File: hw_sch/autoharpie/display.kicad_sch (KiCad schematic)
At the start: 41 parts, among them J5 Conn_01x04_Socket, SW1 RotaryEncoder_Switch, SW19 SW_Push, SW2 RotaryEncoder, SW20 SW_Push, SW21 SW_Push, SW75 RotaryEncoder, SW76 RotaryEncoder

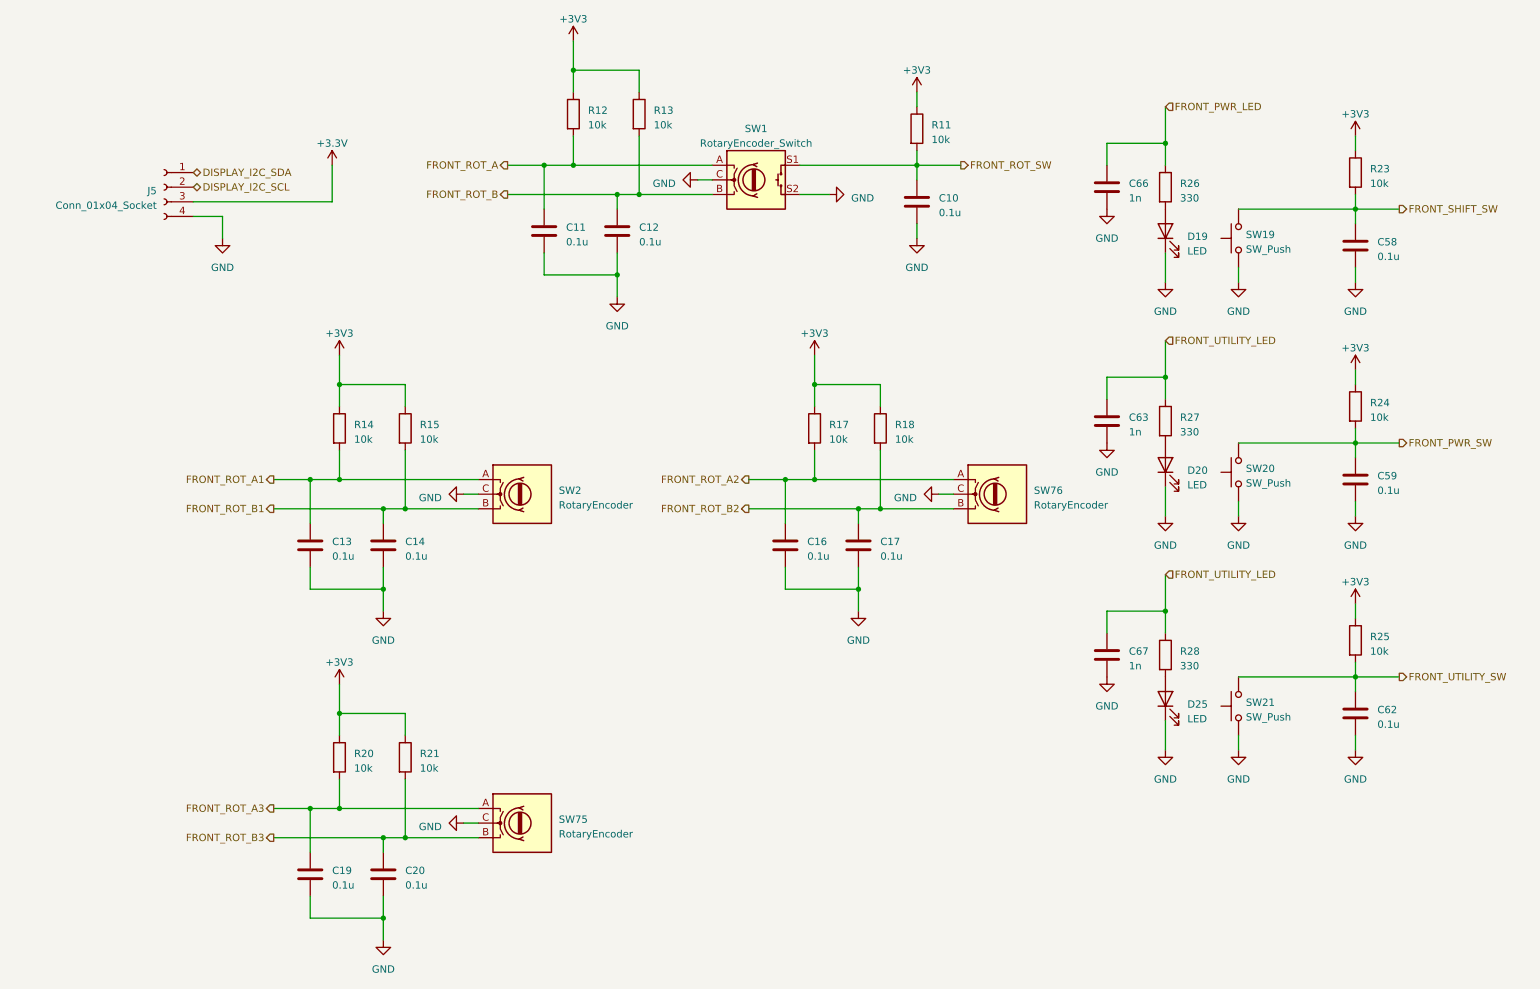
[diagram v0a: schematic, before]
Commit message: DAC wiring, add heirch pins
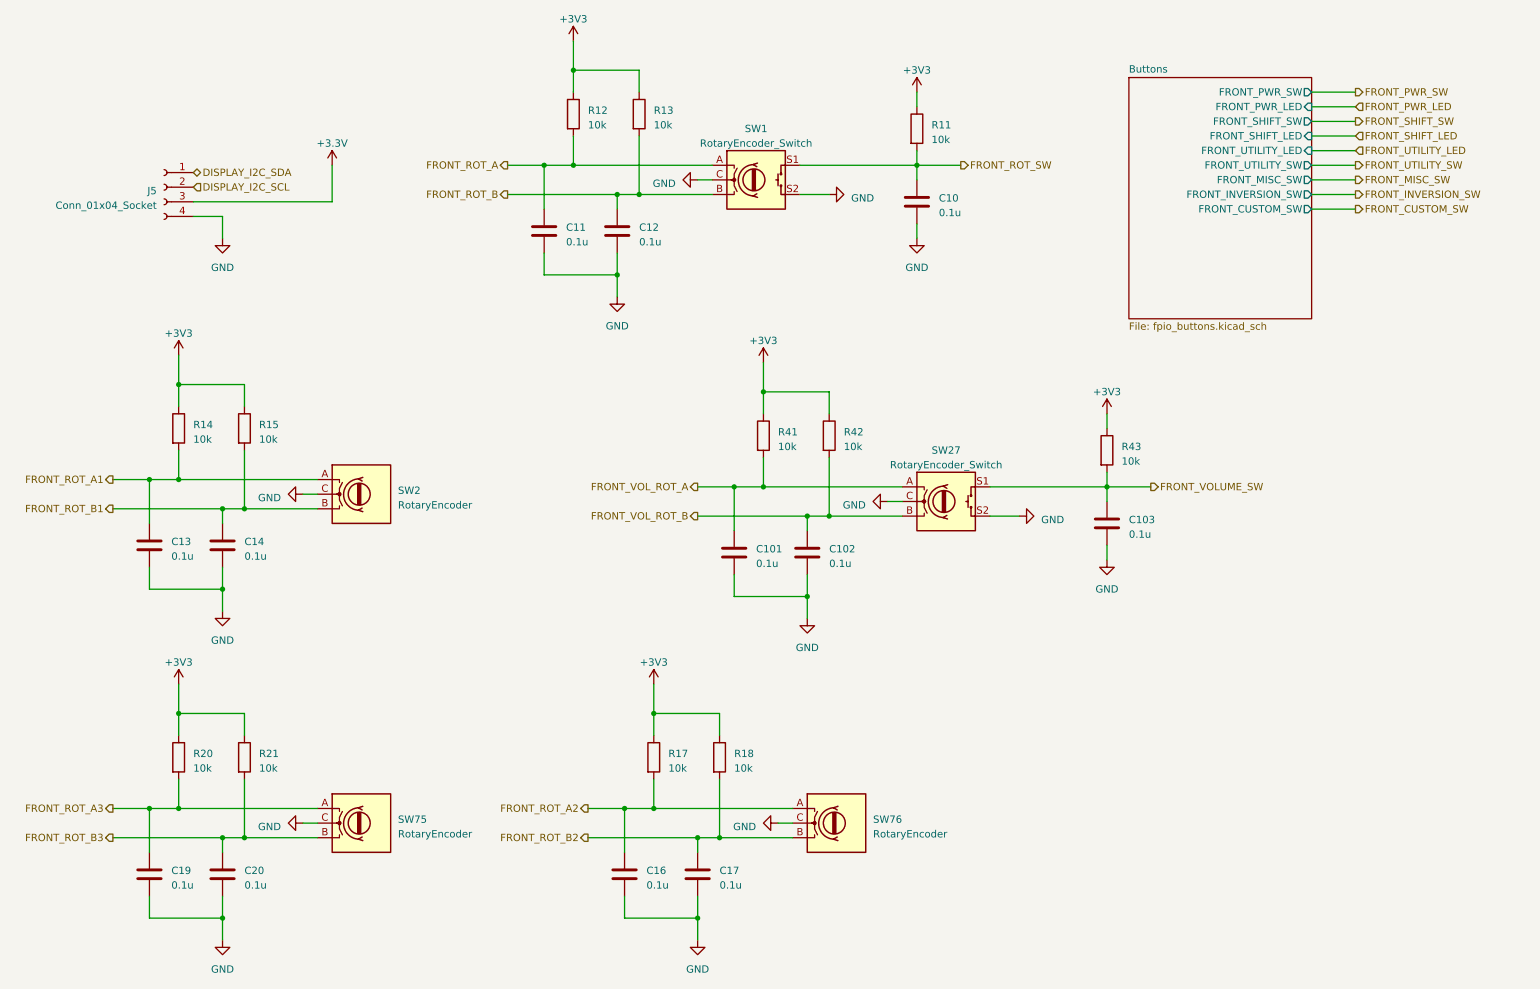
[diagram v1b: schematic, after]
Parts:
- removed C58, C59, C62: 0.1u, symbol Device:C
- removed C63, C66, C67: 1n, symbol Device:C
- removed D19, D20, D25: LED, symbol Device:LED
- removed R23, R24, R25: 10k, symbol Device:R
- removed R26, R27, R28: 330, symbol Device:R
- removed SW19, SW20, SW21: SW_Push, symbol Switch:SW_Push
- added C101, C102, C103: 0.1u, symbol Device:C
- added R41, R42, R43: 10k, symbol Device:R
- added SW27: RotaryEncoder_Switch, symbol Device:RotaryEncoder_Switch
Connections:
- net +3V3: now also R41.1, R42.1, R43.1
- net GND: now also C101.2, C102.2, C103.2, SW27.C, SW27.S2
- new net FRONT_VOLUME_SW: C103.1, R43.2, SW27.S1
- new net FRONT_VOL_ROT_A: C101.1, R41.2, SW27.A
- new net FRONT_VOL_ROT_B: C102.1, R42.2, SW27.B
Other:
- added sheet Buttons (fpio_buttons.kicad_sch)
- moved on the sheet: C13, C14, C16, C17, C19, C20, R14, R15, R17, R18, R20, R21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

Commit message: keypad
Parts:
- removed C101, C102, C103, C13, C14, C16, C17, C19, C20: 0.1u, symbol Device:C
- removed R14, R15, R17, R18, R20, R21, R41, R42, R43: 10k, symbol Device:R
- removed SW2, SW75, SW76: RotaryEncoder, symbol Device:RotaryEncoder
- removed SW27: RotaryEncoder_Switch, symbol Device:RotaryEncoder_Switch
- added C26, C28, C33: 1n, Capacitor_SMD:C_0402_1005Metric, symbol Device:C
- added C27, C29: 0.1u, Capacitor_SMD:C_0402_1005Metric, symbol Device:C
- added D4, D5, D6: LED, LED_THT:LED_D3.0mm, symbol Device:LED
- added R26, R28: 10k, Resistor_THT:R_Axial_DIN0204_L3.6mm_D1.6mm_P7.62mm_Horizontal, symbol Device:R
- added R27, R29, R33: 330, Resistor_THT:R_Axial_DIN0204_L3.6mm_D1.6mm_P7.62mm_Horizontal, symbol Device:R
- added SW1, SW2: SW_Push, Button_Switch_THT:SW_PUSH_6mm_H4.3mm, symbol Switch:SW_Push
- C30: renamed from C10; footprint (none) -> Capacitor_SMD:C_0402_1005Metric
- C31: renamed from C11; footprint (none) -> Capacitor_SMD:C_0402_1005Metric
- C32: renamed from C12; footprint (none) -> Capacitor_SMD:C_0402_1005Metric
- J6: renamed from J5; footprint Display:OLED-128O064D -> Connector_PinSocket_2.54mm:PinSocket_1x04_P2.54mm_Vertical
- R30: renamed from R12; footprint (none) -> Resistor_THT:R_Axial_DIN0204_L3.6mm_D1.6mm_P7.62mm_Horizontal
- R31: renamed from R13; footprint (none) -> Resistor_THT:R_Axial_DIN0204_L3.6mm_D1.6mm_P7.62mm_Horizontal
- R32: renamed from R11; footprint (none) -> Resistor_THT:R_Axial_DIN0204_L3.6mm_D1.6mm_P7.62mm_Horizontal
- SW3: renamed from SW1; footprint (none) -> Rotary_Encoder:RotaryEncoder_Alps_EC11E-Switch_Vertical_H20mm
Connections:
- net +3V3: now also R26.1, R28.1
- net FRONT_PWR_LED: now also C28.1, R29.1
- net FRONT_PWR_SW: now also C29.1, R28.2, SW2.2
- net FRONT_SHIFT_LED: now also C26.1, R27.1
- net FRONT_SHIFT_SW: now also C27.1, R26.2, SW1.2
- net FRONT_UTILITY_LED: now also C33.1, R33.1
- net GND: now also C26.2, C27.2, C28.2, C29.2, C33.2, D4.1 (K), D5.1 (K), D6.1 (K), SW1.1, SW2.1
- new net: D5.2 (A), R29.2
- new net: D6.2 (A), R33.2
- new net: D4.2 (A), R27.2
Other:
- removed sheet Buttons
- moved on the sheet: C30, C31, C32, R30, R31, R32, SW3

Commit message: rev 0.1 pcb
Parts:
- removed C26, C28, C33: 1n, Capacitor_SMD:C_0402_1005Metric, symbol Device:C
- removed C27, C29, C30, C31, C32: 0.1u, Capacitor_SMD:C_0402_1005Metric, symbol Device:C
- removed D4, D5, D6: LED, LED_THT:LED_D3.0mm, symbol Device:LED
- removed R26, R28: 10k, Resistor_THT:R_Axial_DIN0204_L3.6mm_D1.6mm_P7.62mm_Horizontal, symbol Device:R
- removed R27, R29, R33: 330, Resistor_THT:R_Axial_DIN0204_L3.6mm_D1.6mm_P7.62mm_Horizontal, symbol Device:R
- removed SW1, SW2: SW_Push, Button_Switch_THT:SW_PUSH_6mm_H4.3mm, symbol Switch:SW_Push
- renumbered J6 to J4, R30 to R10, R31 to R11, R32 to R12, SW3 to SW1
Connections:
- net +3.3V is gone; now on net DISPLAY_I2C_SCL: J4.3 (Pin_3)
- net +3V3: now also J4.2 (Pin_2)
- net DISPLAY_I2C_SCL: no longer J4.2 (Pin_2)
- net DISPLAY_I2C_SDA: now also J4.4 (Pin_4); no longer J4.1 (Pin_1)
- net GND: now also J4.1 (Pin_1); no longer J4.4 (Pin_4)

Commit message: ic fix atept
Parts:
- SW2: renamed from SW1; footprint Rotary_Encoder:RotaryEncoder_Alps_EC11E-Switch_Vertical_H20mm -> Rotary_Encoder:RotaryEncoder_Bourns_Vertical_PEC12R-3xxxF-Sxxxx
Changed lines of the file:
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@@
   (symbol (lib_id "power:GND") (at 77.47 100.33 270) (unit 1)
     (in_bom yes) (on_board yes) (dnp no) (fields_autoplaced)
-    (property "Reference" "#PWR045" (at 71.12 100.33 0)
+    (property "Reference" "#PWR047" (at 71.12 100.33 0)
       (effects (font (size 1.27 1.27)) hide)
     )
@@
       (project "autoharpie"
         (path "/f22a88c4-866b-40a0-9fc2-96344be0ec71/b98961c6-5a9e-45f8-94a5-02c3a7ae5bfc"
+          (reference "#PWR047") (unit 1)
+        )
+      )
+    )
+  )
+  (symbol (lib_id "power:+3V3") (at 45.72 48.26 270) (unit 1)
+    (in_bom yes) (on_board yes) (dnp no) (fields_autoplaced)
+    (property "Reference" "#PWR044" (at 41.91 48.26 0)
+      (effects (font (size 1.27 1.27)) hide)
+    )
+    (property "Value" "+3V3" (at 49.53 48.895 90)
+      (effects (font (size 1.27 1.27)) (justify left))
+    )
+    (property "Footprint" "" (at 45.72 48.26 0)
+      (effects (font (size 1.27 1.27)) hide)
+    )
+    (property "Datasheet" "" (at 45.72 48.26 0)
+      (effects (font (size 1.27 1.27)) hide)
+    )
+    (pin "1")
+    (instances
+      (project "autoharpie"
+        (path "/f22a88c4-866b-40a0-9fc2-96344be0ec71/b98961c6-5a9e-45f8-94a5-02c3a7ae5bfc"
+          (reference "#PWR044") (unit 1)
+        )
+      )
+    )
+  )
+  (symbol (lib_id "Device:R") (at 55.88 88.9 0) (unit 1)
+    (in_bom yes) (on_board yes) (dnp no) (fields_autoplaced)
+    (property "Reference" "R10" (at 58.42 88.265 0)
+      (effects (font (size 1.27 1.27)) (justify left))
+    )
+    (property "Value" "10k" (at 58.42 90.805 0)
+      (effects (font (size 1.27 1.27)) (justify left))
+    )
+    (property "Footprint" "Resistor_THT:R_Axial_DIN0204_L3.6mm_D1.6mm_P7.62mm_Horizontal" (at 54.102 88.9 90)
+      (effects (font (size 1.27 1.27)) hide)
+    )
+    (property "Datasheet" "~" (at 55.88 88.9 0)
+      (effects (font (size 1.27 1.27)) hide)
+    )
+    (pin "1")
+    (pin "2")
+    (instances
+      (project "autoharpie"
+        (path "/f22a88c4-866b-40a0-9fc2-96344be0ec71/b98961c6-5a9e-45f8-94a5-02c3a7ae5bfc"
+          (reference "R10") (unit 1)
+        )
+      )
+    )
+  )
+  (symbol (lib_id "Device:R") (at 67.31 88.9 0) (unit 1)
+    (in_bom yes) (on_board yes) (dnp no) (fields_autoplaced)
+    (property "Reference" "R11" (at 69.85 88.265 0)
+      (effects (font (size 1.27 1.27)) (justify left))
+    )
+    (property "Value" "10k" (at 69.85 90.805 0)
+      (effects (font (size 1.27 1.27)) (justify left))
+    )
+    (property "Footprint" "Resistor_THT:R_Axial_DIN0204_L3.6mm_D1.6mm_P7.62mm_Horizontal" (at 65.532 88.9 90)
+      (effects (font (size 1.27 1.27)) hide)
+    )
+    (property "Datasheet" "~" (at 67.31 88.9 0)
+      (effects (font (size 1.27 1.27)) hide)
+    )
+    (pin "1")
+    (pin "2")
+    (instances
+      (project "autoharpie"
+        (path "/f22a88c4-866b-40a0-9fc2-96344be0ec71/b98961c6-5a9e-45f8-94a5-02c3a7ae5bfc"
+          (reference "R11") (unit 1)
+        )
+      )
+    )
+  )
+  (symbol (lib_id "power:+3V3") (at 55.88 76.2 0) (unit 1)
+    (in_bom yes) (on_board yes) (dnp no) (fields_autoplaced)
+    (property "Reference" "#PWR045" (at 55.88 80.01 0)
+      (effects (font (size 1.27 1.27)) hide)
+    )
+    (property "Value" "+3V3" (at 55.88 72.39 0)
+      (effects (font (size 1.27 1.27)))
+    )
+    (property "Footprint" "" (at 55.88 76.2 0)
+      (effects (font (size 1.27 1.27)) hide)
+    )
+    (property "Datasheet" "" (at 55.88 76.2 0)
+      (effects (font (size 1.27 1.27)) hide)
+    )
+    (pin "1")
+    (instances
+      (project "autoharpie"
+        (path "/f22a88c4-866b-40a0-9fc2-96344be0ec71/b98961c6-5a9e-45f8-94a5-02c3a7ae5bfc"
           (reference "#PWR045") (unit 1)
         )
@@
     )
   )
-  (symbol (lib_id "power:+3V3") (at 45.72 48.26 270) (unit 1)
-    (in_bom yes) (on_board yes) (dnp no) (fields_autoplaced)
-    (property "Reference" "#PWR042" (at 41.91 48.26 0)
-      (effects (font (size 1.27 1.27)) hide)
-    )
-    (property "Value" "+3V3" (at 49.53 48.895 90)
-      (effects (font (size 1.27 1.27)) (justify left))
-    )
-    (property "Footprint" "" (at 45.72 48.26 0)
-      (effects (font (size 1.27 1.27)) hide)
-    )
-    (property "Datasheet" "" (at 45.72 48.26 0)
-      (effects (font (size 1.27 1.27)) hide)
-    )
-    (pin "1")
-    (instances
-      (project "autoharpie"
-        (path "/f22a88c4-866b-40a0-9fc2-96344be0ec71/b98961c6-5a9e-45f8-94a5-02c3a7ae5bfc"
-          (reference "#PWR042") (unit 1)
-        )
-      )
-    )
-  )
-  (symbol (lib_id "Device:R") (at 55.88 88.9 0) (unit 1)
-    (in_bom yes) (on_board yes) (dnp no) (fields_autoplaced)
-    (property "Reference" "R10" (at 58.42 88.265 0)
-      (effects (font (size 1.27 1.27)) (justify left))
-    )
-    (property "Value" "10k" (at 58.42 90.805 0)
-      (effects (font (size 1.27 1.27)) (justify left))
-    )
-    (property "Footprint" "Resistor_THT:R_Axial_DIN0204_L3.6mm_D1.6mm_P7.62mm_Horizontal" (at 54.102 88.9 90)
-      (effects (font (size 1.27 1.27)) hide)
-    )
-    (property "Datasheet" "~" (at 55.88 88.9 0)
-      (effects (font (size 1.27 1.27)) hide)
-    )
-    (pin "1")
-    (pin "2")
-    (instances
-      (project "autoharpie"
-        (path "/f22a88c4-866b-40a0-9fc2-96344be0ec71/b98961c6-5a9e-45f8-94a5-02c3a7ae5bfc"
-          (reference "R10") (unit 1)
-        )
-      )
-    )
-  )
-  (symbol (lib_id "Device:R") (at 67.31 88.9 0) (unit 1)
-    (in_bom yes) (on_board yes) (dnp no) (fields_autoplaced)
-    (property "Reference" "R11" (at 69.85 88.265 0)
-      (effects (font (size 1.27 1.27)) (justify left))
-    )
-    (property "Value" "10k" (at 69.85 90.805 0)
-      (effects (font (size 1.27 1.27)) (justify left))
-    )
-    (property "Footprint" "Resistor_THT:R_Axial_DIN0204_L3.6mm_D1.6mm_P7.62mm_Horizontal" (at 65.532 88.9 90)
-      (effects (font (size 1.27 1.27)) hide)
-    )
-    (property "Datasheet" "~" (at 67.31 88.9 0)
-      (effects (font (size 1.27 1.27)) hide)
-    )
-    (pin "1")
-    (pin "2")
-    (instances
-      (project "autoharpie"
-        (path "/f22a88c4-866b-40a0-9fc2-96344be0ec71/b98961c6-5a9e-45f8-94a5-02c3a7ae5bfc"
-          (reference "R11") (unit 1)
-        )
-      )
-    )
-  )
-  (symbol (lib_id "power:+3V3") (at 55.88 76.2 0) (unit 1)
-    (in_bom yes) (on_board yes) (dnp no) (fields_autoplaced)
-    (property "Reference" "#PWR043" (at 55.88 80.01 0)
-      (effects (font (size 1.27 1.27)) hide)
-    )
-    (property "Value" "+3V3" (at 55.88 72.39 0)
-      (effects (font (size 1.27 1.27)))
-    )
-    (property "Footprint" "" (at 55.88 76.2 0)
-      (effects (font (size 1.27 1.27)) hide)
-    )
-    (property "Datasheet" "" (at 55.88 76.2 0)
-      (effects (font (size 1.27 1.27)) hide)
-    )
-    (pin "1")
-    (instances
-      (project "autoharpie"
-        (path "/f22a88c4-866b-40a0-9fc2-96344be0ec71/b98961c6-5a9e-45f8-94a5-02c3a7ae5bfc"
-          (reference "#PWR043") (unit 1)
-        )
-      )
-    )
-  )
   (symbol (lib_id "Device:RotaryEncoder_Switch") (at 87.63 100.33 0) (unit 1)
     (in_bom yes) (on_board yes) (dnp no) (fields_autoplaced)
-    (property "Reference" "SW1" (at 87.63 91.44 0)
+    (property "Reference" "SW2" (at 87.63 91.44 0)
       (effects (font (size 1.27 1.27)))
     )
@@
       (effects (font (size 1.27 1.27)))
     )
-    (property "Footprint" "Rotary_Encoder:RotaryEncoder_Alps_EC11E-Switch_Vertical_H20mm" (at 83.82 96.266 0)
+    (property "Footprint" "Rotary_Encoder:RotaryEncoder_Bourns_Vertical_PEC12R-3xxxF-Sxxxx" (at 83.82 96.266 0)
       (effects (font (size 1.27 1.27)) hide)
     )
@@
       (project "autoharpie"
         (path "/f22a88c4-866b-40a0-9fc2-96344be0ec71/b98961c6-5a9e-45f8-94a5-02c3a7ae5bfc"
-          (reference "SW1") (unit 1)
+          (reference "SW2") (unit 1)
         )
       )
@@
   (symbol (lib_id "power:+3V3") (at 123.19 85.09 0) (unit 1)
     (in_bom yes) (on_board yes) (dnp no) (fields_autoplaced)
-    (property "Reference" "#PWR044" (at 123.19 88.9 0)
+    (property "Reference" "#PWR046" (at 123.19 88.9 0)
       (effects (font (size 1.27 1.27)) hide)
     )
@@
       (project "autoharpie"
         (path "/f22a88c4-866b-40a0-9fc2-96344be0ec71/b98961c6-5a9e-45f8-94a5-02c3a7ae5bfc"
-          (reference "#PWR044") (unit 1)
+          (reference "#PWR046") (unit 1)
         )
       )
@@
   (symbol (lib_id "power:GND") (at 45.72 45.72 90) (unit 1)
     (in_bom yes) (on_board yes) (dnp no) (fields_autoplaced)
-    (property "Reference" "#PWR041" (at 52.07 45.72 0)
+    (property "Reference" "#PWR043" (at 52.07 45.72 0)
       (effects (font (size 1.27 1.27)) hide)
     )
@@
       (project "autoharpie"
         (path "/f22a88c4-866b-40a0-9fc2-96344be0ec71/b98961c6-5a9e-45f8-94a5-02c3a7ae5bfc"
-          (reference "#PWR041") (unit 1)
+          (reference "#PWR043") (unit 1)
         )
       )
@@
   (symbol (lib_id "power:GND") (at 100.33 102.87 90) (unit 1)
     (in_bom yes) (on_board yes) (dnp no) (fields_autoplaced)
-    (property "Reference" "#PWR046" (at 106.68 102.87 0)
+    (property "Reference" "#PWR048" (at 106.68 102.87 0)
       (effects (font (size 1.27 1.27)) hide)
     )
@@
       (project "autoharpie"
         (path "/f22a88c4-866b-40a0-9fc2-96344be0ec71/b98961c6-5a9e-45f8-94a5-02c3a7ae5bfc"
-          (reference "#PWR046") (unit 1)
-        )
-      )
+          (reference "#PWR048") (unit 1)
+        )
+      )
